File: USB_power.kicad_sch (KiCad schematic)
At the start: 25 parts, among them J1 JST-4-pin, J1 TYPE-C-31-M12_13, SW1 MK-12C02-G025, U1 BQ24074RGTR, U2 AP2127K-3.0TRG1, U4 TPD4E05U06DQAR

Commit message: gerber generated
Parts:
- U2: value AP2127K-3.0TRG1 -> AP2127K-3.3TRG1; LCSC Part Number C460328 -> C156285; LCSC link https://www.lcsc.com/product-detail/Linear-Voltage-Regulators-LDO_Diodes-Incorporated-AP2127K-3-0TRG1_C460328.html -> https://www.lcsc.com/product-detail/Linear-Voltage-Regulators-LDO_Diodes-Incorporated-AP2127K-3-3TRG1_C156285.html; PN AP2127K-3.0TRG1 -> AP2127K-3.3TRG1
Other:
- note added: "A SPDT switch is used to select power source. Switch position 1 - Direct power from USB connector. Switch position 2 - Power from battery and USB connector. If anybody wants to use keyboard without battery and cahrger module can do so by putting the switch in position 1. If anyone wants to use keyboard with only usb power, The whole BQ24074 section can be made DNP and SW1 can be slided to POS 1 t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"
- note added: "Riterm (R5) = 5k1 sets termination current to 125mA"
- note added: "Theere are 3 charger IC which are functionally compatibility. BQ24073, BQ24074, BQ24075. Any one of thrm can be used. They are all pin to pin compatible and the design is done in such a way that you can swap out one for another on same PCB and have same functionality."
- note removed: "A SPDT switch is used to select power source. Switch position 1 - Direct power from USB connector. Switch position 2 - Power from battery and USB connector. If anybody wants to use keyboard without battery and cahrger module can do so by putting the switch in position 1. If battery is connected, then put it to position 2."
- note removed: "Riterm (R5) = 2k sets termination current to 50mA"
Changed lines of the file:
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@@
   (junction (at 218.44 41.91) (diameter 0) (color 0 0 0 0)
+  )
+  (junction (at 251.46 110.49) (diameter 0) (color 0 0 0 0)
   )
   (junction (at 102.87 124.46) (diameter 0) (color 0 0 0 0)
@@
     (stroke (width 0) (type default))
   )
+  (wire (pts (xy 251.46 110.49) (xy 257.81 110.49))
+    (stroke (width 0) (type default))
+  )
   (wire (pts (xy 243.84 52.07) (xy 243.84 54.61))
     (stroke (width 0) (type default))
@@
     (stroke (width 0) (type default))
   )
+  (wire (pts (xy 243.84 41.91) (xy 243.84 44.45))
+    (stroke (width 0) (type default))
+  )
+  (wire (pts (xy 132.08 110.49) (xy 132.08 114.3))
+    (stroke (width 0) (type default))
+  )
+  (wire (pts (xy 251.46 116.84) (xy 251.46 119.38))
+    (stroke (width 0) (type default))
+  )
+  (wire (pts (xy 102.87 123.19) (xy 102.87 124.46))
+    (stroke (width 0) (type default))
+  )
+  (wire (pts (xy 62.23 125.73) (xy 58.42 125.73))
+    (stroke (width 0) (type default))
+  )
+  (wire (pts (xy 115.57 114.3) (xy 120.65 114.3))
+    (stroke (width 0) (type default))
+  )
+  (wire (pts (xy 97.79 135.89) (xy 100.33 135.89))
+    (stroke (width 0) (type default))
+  )
+  (wire (pts (xy 64.77 184.15) (xy 76.2 184.15))
+    (stroke (width 0) (type default))
+  )
+  (wire (pts (xy 34.925 140.97) (xy 34.925 138.43))
+    (stroke (width 0) (type default))
+  )
+  (wire (pts (xy 77.47 153.67) (xy 77.47 157.48))
+    (stroke (width 0) (type default))
+  )
+  (wire (pts (xy 106.68 130.81) (xy 106.68 124.46))
+    (stroke (width 0) (type default))
+  )
+  (wire (pts (xy 128.27 114.3) (xy 132.08 114.3))
+    (stroke (width 0) (type default))
+  )
+  (wire (pts (xy 58.42 128.27) (xy 62.23 128.27))
+    (stroke (width 0) (type default))
+  )
+  (wire (pts (xy 39.37 121.92) (xy 39.37 123.19))
+    (stroke (width 0) (type default))
+  )
+  (wire (pts (xy 52.07 133.35) (xy 52.07 143.51))
+    (stroke (width 0) (type default))
+  )
+  (wire (pts (xy 149.86 48.26) (xy 156.21 48.26))
+    (stroke (width 0) (type default))
+  )
+  (wire (pts (xy 34.925 138.43) (xy 46.355 138.43))
+    (stroke (width 0) (type default))
+  )
+  (wire (pts (xy 27.94 115.57) (xy 39.37 115.57))
+    (stroke (width 0) (type default))
+  )
+  (wire (pts (xy 49.53 91.44) (xy 46.99 91.44))
+    (stroke (width 0) (type default))
+  )
   (wire (pts (xy 251.46 110.49) (xy 251.46 111.76))
     (stroke (width 0) (type default))
   )
-  (wire (pts (xy 243.84 41.91) (xy 243.84 44.45))
-    (stroke (width 0) (type default))
-  )
-  (wire (pts (xy 132.08 110.49) (xy 132.08 114.3))
-    (stroke (width 0) (type default))
-  )
-  (wire (pts (xy 251.46 116.84) (xy 251.46 119.38))
-    (stroke (width 0) (type default))
-  )
-  (wire (pts (xy 102.87 123.19) (xy 102.87 124.46))
-    (stroke (width 0) (type default))
-  )
-  (wire (pts (xy 62.23 125.73) (xy 58.42 125.73))
-    (stroke (width 0) (type default))
-  )
-  (wire (pts (xy 115.57 114.3) (xy 120.65 114.3))
-    (stroke (width 0) (type default))
-  )
-  (wire (pts (xy 97.79 135.89) (xy 100.33 135.89))
-    (stroke (width 0) (type default))
-  )
-  (wire (pts (xy 64.77 184.15) (xy 76.2 184.15))
-    (stroke (width 0) (type default))
-  )
-  (wire (pts (xy 34.925 140.97) (xy 34.925 138.43))
-    (stroke (width 0) (type default))
-  )
-  (wire (pts (xy 77.47 153.67) (xy 77.47 157.48))
-    (stroke (width 0) (type default))
-  )
-  (wire (pts (xy 106.68 130.81) (xy 106.68 124.46))
-    (stroke (width 0) (type default))
-  )
-  (wire (pts (xy 128.27 114.3) (xy 132.08 114.3))
-    (stroke (width 0) (type default))
-  )
-  (wire (pts (xy 58.42 128.27) (xy 62.23 128.27))
-    (stroke (width 0) (type default))
-  )
-  (wire (pts (xy 39.37 121.92) (xy 39.37 123.19))
-    (stroke (width 0) (type default))
-  )
-  (wire (pts (xy 52.07 133.35) (xy 52.07 143.51))
-    (stroke (width 0) (type default))
-  )
-  (wire (pts (xy 149.86 48.26) (xy 156.21 48.26))
-    (stroke (width 0) (type default))
-  )
-  (wire (pts (xy 34.925 138.43) (xy 46.355 138.43))
-    (stroke (width 0) (type default))
-  )
-  (wire (pts (xy 27.94 115.57) (xy 39.37 115.57))
-    (stroke (width 0) (type default))
-  )
-  (wire (pts (xy 49.53 91.44) (xy 46.99 91.44))
-    (stroke (width 0) (type default))
-  )
   (wire (pts (xy 39.37 116.84) (xy 39.37 115.57))
     (stroke (width 0) (type default))
@@
   )
   (text "Voltage divider to \nmeasure battery voltage.\n\n" (at 156.845 102.87 0)
+    (effects (font (size 1.27 1.27)) (justify left bottom))
+  )
+  (text "Theere are 3 charger IC which are\nfunctionally compatibility.\nBQ24073, BQ24074, BQ24075.\nAny one of thrm can be used.\nThey are all pin to pin compatible \nand the design is done in such a way\nthat you can swap out one for another \non same PCB and have same functionality."
+    (at 58.42 106.68 0)
     (effects (font (size 1.27 1.27)) (justify left bottom))
   )
@@
     (effects (font (size 1.27 1.27)) (justify left bottom))
   )
-  (text "Riterm (R5) = 2k \nsets termination \ncurrent to 50mA"
+  (text "Riterm (R5) = 5k1 \nsets termination \ncurrent to 125mA"
     (at 99.06 153.67 0)
     (effects (font (size 1.27 1.27) bold) (justify left bottom))
@@
     (effects (font (size 2 2) (thickness 0.4) bold) (justify left bottom))
   )
-  (text "HERE" (at 101.6 63.5 0)
+  (text "HERE" (at 101.6 64.77 0)
     (effects (font (size 2 2) (thickness 0.254) bold) (justify left bottom) (href "https://unified-daughterboard.github.io/#/?id=unified-daughterboard"))
   )
@@
     (effects (font (size 1.27 1.27) bold) (justify left bottom))
   )
-  (text "A SPDT switch is used to select power source.\nSwitch position 1 - Direct power from USB connector.\nSwitch position 2 - Power from battery and USB connector.\n\nIf anybody wants to use keyboard without battery and\ncahrger module can do so by putting the switch in \nposition 1. \n\nIf battery is connected, then put it to position 2."
-    (at 138.43 73.66 0)
+  (text "A SPDT switch is used to select power source.\nSwitch position 1 - Direct power from USB connector.\nSwitch position 2 - Power from battery and USB connector.\n\nIf anybody wants to use keyboard without battery and\ncahrger module can do so by putting the switch in \nposition 1. \n\nIf anyone wants to use keyboard with only usb power,\nThe whole BQ24074 section can be made DNP and SW1 \ncan be slided to POS 1 to operate only with USB\nwithout Battery.\n\nIf battery is connected, then put it to position 2."
+    (at 142.24 85.09 0)
     (effects (font (size 1.27 1.27) bold) (justify left bottom))
   )
@@
     (effects (font (size 1.27 1.27)) (justify left bottom))
   )
-  (label "3V3" (at 251.46 110.49 180) (fields_autoplaced)
+  (label "3V3" (at 257.81 110.49 180) (fields_autoplaced)
     (effects (font (size 1.27 1.27) bold) (justify right bottom))
   )
@@
       (effects (font (size 1.27 1.27)))
     )
-    (property "Value" "AP2127K-3.0TRG1" (at 231.14 106.68 0)
+    (property "Value" "AP2127K-3.3TRG1" (at 231.14 106.68 0)
       (effects (font (size 1.27 1.27)))
     )
@@
       (effects (font (size 1.27 1.27)) hide)
     )
-    (property "Datasheet" "https://datasheet.lcsc.com/lcsc/2304140030_Diodes-Incorporated-AP2125K-3-3TRG1_C110463.pdf" (at 231.14 115.57 0)
-      (effects (font (size 1.27 1.27)) hide)
-    )
-    (property "PN" "AP2127K-3.0TRG1" (at 231.14 115.57 0)
-      (effects (font (size 1.27 1.27)) hide)
-    )
-    (property "LCSC link" "https://www.lcsc.com/product-detail/Linear-Voltage-Regulators-LDO_Diodes-Incorporated-AP2127K-3-0TRG1_C460328.html" (at 231.14 115.57 0)
-      (effects (font (size 1.27 1.27)) hide)
-    )
-    (property "LCSC Part Number" "C460328" (at 231.14 115.57 0)
-      (effects (font (size 1.27 1.27)) hide)
-    )
+    (property "Datasheet" "https://datasheet.lcsc.com/lcsc/2304140030_Diodes-Incorporated-AP2127K-3-3TRG1_C156285.pdf" (at 231.14 115.57 0)
+      (effects (font (size 1.27 1.27)) hide)
+    )
+    (property "PN" "AP2127K-3.3TRG1" (at 231.14 115.57 0)
+      (effects (font (size 1.27 1.27)) hide)
+    )
+    (property "LCSC link" "https://www.lcsc.com/product-detail/Linear-Voltage-Regulators-LDO_Diodes-Incorporated-AP2127K-3-3TRG1_C156285.html" (at 231.14 115.57 0)
+      (effects (font (size 1.27 1.27)) hide)
+    )
+    (property "LCSC Part Number" "C156285" (at 231.14 115.57 0)
+      (effects (font (size 1.27 1.27)) hide)
+    )

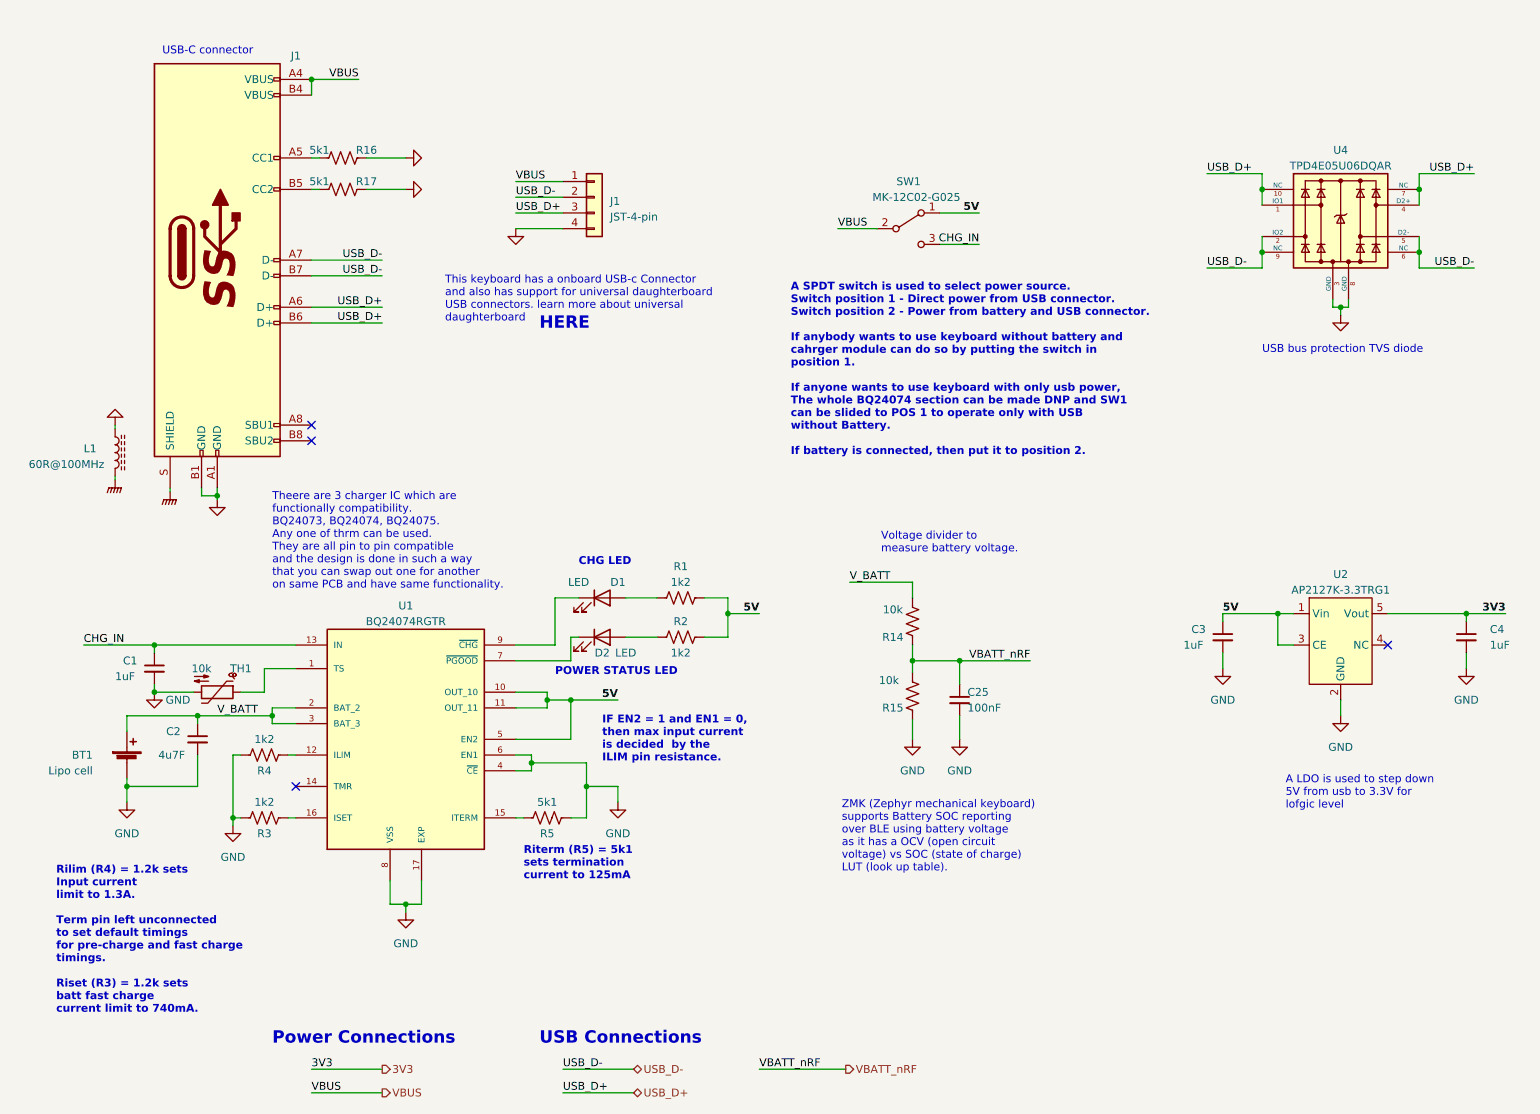
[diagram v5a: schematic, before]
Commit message: Made changes to add support for salvation keyboard case and discord reviews implemented
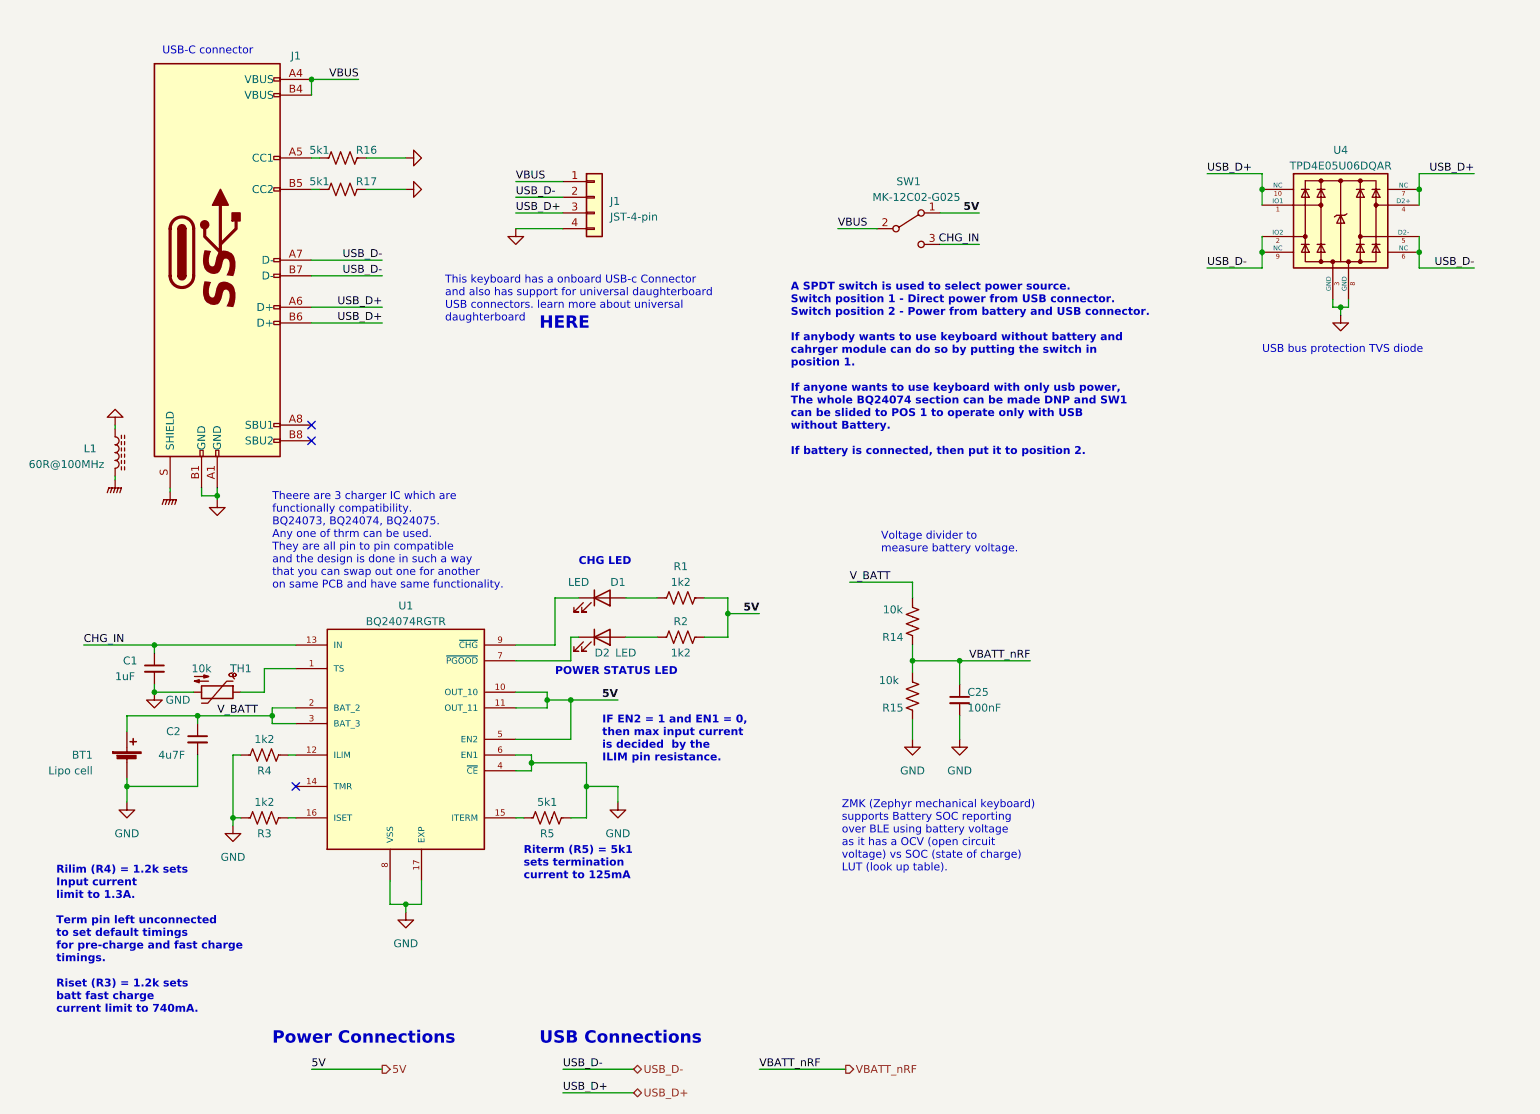
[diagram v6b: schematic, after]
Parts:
- removed C3, C4: 1uF, keyboard:C_0603_1608Metric, symbol Device:C_Small
- removed U2: AP2127K-3.3TRG1, keyboard:SOT-23-5, symbol keyboard:AP2125K-3.3TRG1_
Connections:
- no-connect marks 4 -> 3
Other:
- note removed: "A LDO is used to step down 5V from usb to 3.3V for lofgic level"
